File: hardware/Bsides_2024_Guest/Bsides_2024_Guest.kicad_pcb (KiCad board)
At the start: 2 copper layers, 0 parts

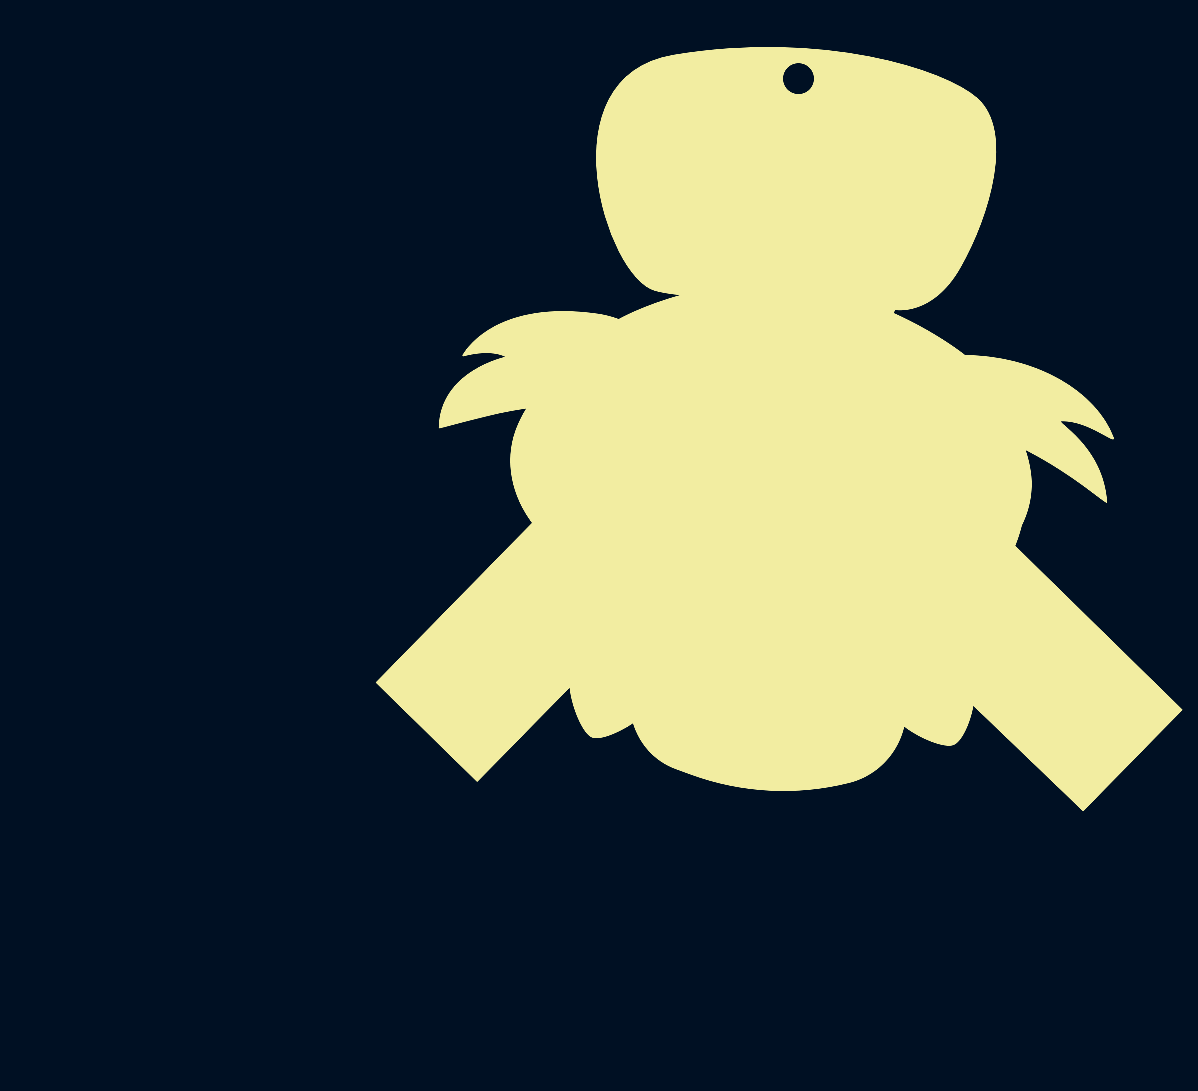
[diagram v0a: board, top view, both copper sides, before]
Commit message: feat(Hw):Added_Guest_And_Sponsor_Floorplan_and_3d_Models
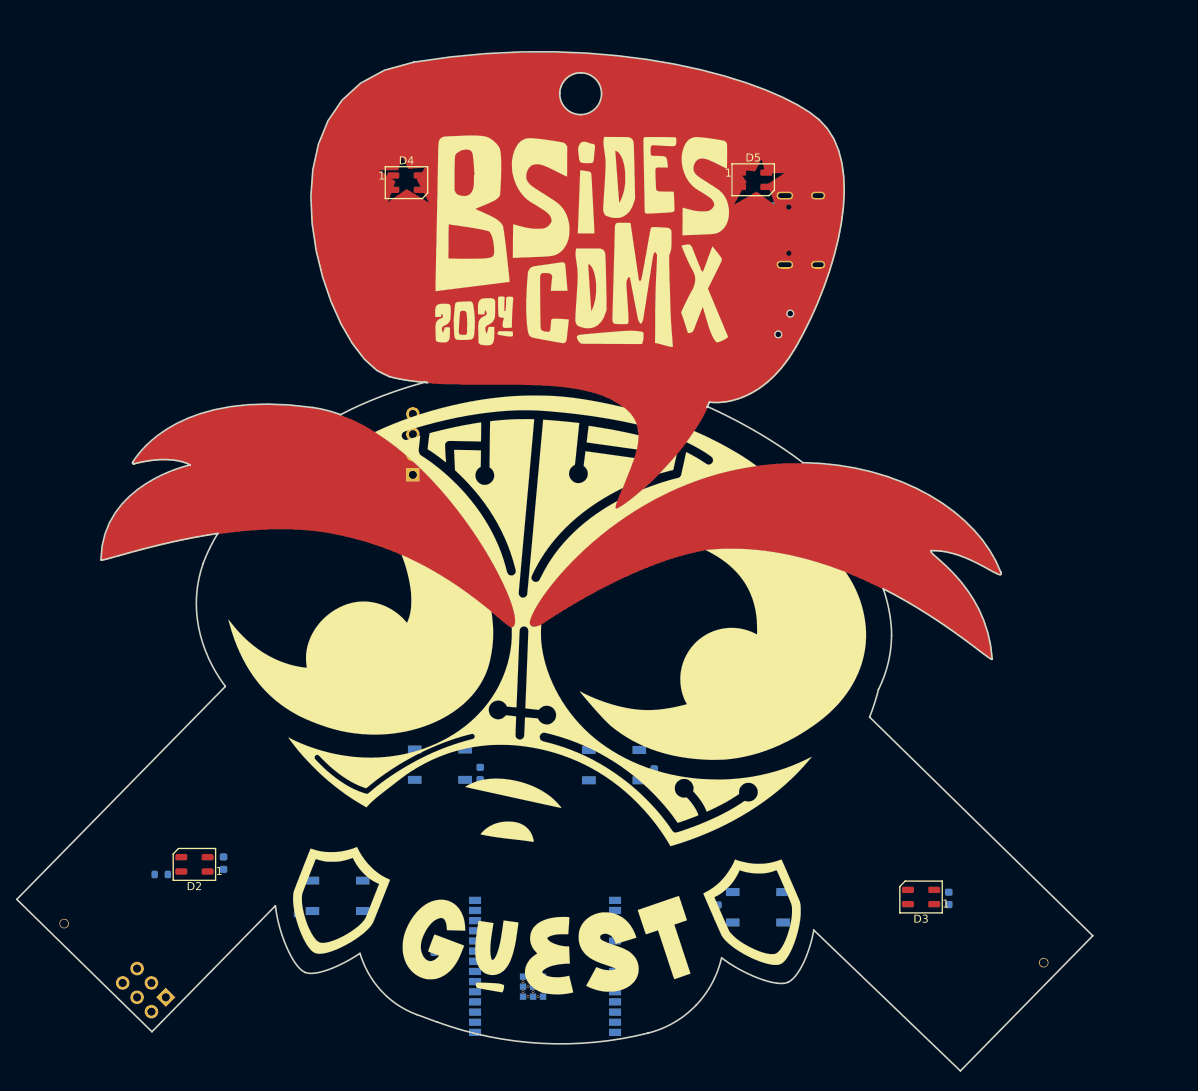
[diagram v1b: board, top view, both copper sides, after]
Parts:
- added C1: 10uF, Capacitor_SMD:C_0603_1608Metric, B.Cu at (149.0, 66.2)
- added C10: 0.1uF, Capacitor_SMD:C_0603_1608Metric, B.Cu at (116.2, 116.2)
- added C11: 0.1uF, Capacitor_SMD:C_0603_1608Metric, B.Cu at (145.9, 133.4)
- added C12: 0.1uF, Capacitor_SMD:C_0603_1608Metric, B.Cu at (146.8, 41.7)
- added C2: 10uF, Capacitor_SMD:C_0603_1608Metric, B.Cu at (143.4, 66.2)
- added C3: 0.1uF, Capacitor_SMD:C_0603_1608Metric, B.Cu at (168.6, 90.5)
- added C4: 0.1uF, Capacitor_SMD:C_0603_1608Metric, B.Cu at (85.2, 79.4)
- added C5: 0.1uF, Capacitor_SMD:C_0603_1608Metric, B.Cu at (84.1, 127.4)
- added C6: 0.1uF, Capacitor_SMD:C_0603_1608Metric, B.Cu at (174.8, 131.8)
- added C7: 0.1uF, Capacitor_SMD:C_0603_1608Metric, B.Cu at (103.5, 42.5)
- added C8: 0.1uF, Capacitor_SMD:C_0603_1608Metric, B.Cu at (137.9, 116.4)
- added C9: 0.1uF, Capacitor_SMD:C_0603_1608Metric, B.Cu at (93.3, 133.0)
- added D1: MBR120, Diode_SMD:D_SOD-123F, B.Cu at (144.0, 60.4)
- added D2: WS2812B, LED_SMD:LED_WS2812B-Mini_PLCC4_3.5x3.5mm, F.Cu at (80.5, 127.6)
- added D3: WS2812B, LED_SMD:LED_WS2812B-Mini_PLCC4_3.5x3.5mm, F.Cu at (171.3, 131.7)
- added D4: WS2812B, LED_SMD:LED_WS2812B-Mini_PLCC4_3.5x3.5mm, F.Cu at (107.0, 42.4)
- added D5: WS2812B, LED_SMD:LED_WS2812B-Mini_PLCC4_3.5x3.5mm, F.Cu at (150.3, 42.0)
- added F1: 0.5A, Fuse:Fuse_0805_2012Metric, B.Cu at (148.8, 51.8)
- added J1: Conn_02x03_Odd_Even, Connector_PinSocket_2.54mm:PinSocket_2x03_P2.54mm_Vertical, B.Cu at (76.9, 144.2)
- added J2: Battery, bsides:BH-AAA-A1aj001, B.Cu at (170.5, 123.8)
- added J3: Battery, bsides:BH-AAA-A1aj001, B.Cu at (80.3, 118.9)
- added J4: OLED, bsides:Display OLED 128 x32, B.Cu at (107.8, 78.9)
- added P1: USB_C_Plug_USB2.0, bsides:C393939, B.Cu at (154.3, 48.3)
- added Q1: DMG3415U-7, Package_TO_SOT_SMD:SOT-23, B.Cu at (146.9, 58.7)
- added R1: 3.3K, Resistor_SMD:R_0603_1608Metric, B.Cu at (110.4, 139.5)
- added R2: 100K, Resistor_SMD:R_0603_1608Metric, B.Cu at (142.1, 59.8)
- added R3: 5k1, Resistor_SMD:R_0603_1608Metric, B.Cu at (148.9, 49.2)
- added R4: 5k1, Resistor_SMD:R_0603_1608Metric, B.Cu at (148.9, 46.7)
- added R5: 10K, Resistor_SMD:R_0603_1608Metric, B.Cu at (88.3, 79.5)
- added R6: 470, Resistor_SMD:R_0603_1608Metric, B.Cu at (76.3, 128.9)
- added Ref**: Val**, Guest:Badge Guest, F.Cu at (125.6, 89.8)
- added SW1: ON, bsides:MSK12C02, B.Cu at (154.2, 60.0)
- added SW2: RESET, Button_Switch_SMD:SW_SPST_TL3342, B.Cu at (88.3, 75.5)
- added SW3: BOOT, Button_Switch_SMD:SW_SPST_TL3342, B.Cu at (167.8, 85.6)
- added SW4: RESET, Button_Switch_SMD:SW_SPST_TL3342, B.Cu at (132.9, 115.2)
- added SW5: ~, Button_Switch_SMD:SW_SPST_TL3342, B.Cu at (98.3, 131.5)
- added SW6: RESET, Button_Switch_SMD:SW_SPST_TL3342, B.Cu at (111.1, 115.1)
- added SW7: ~, Button_Switch_SMD:SW_SPST_TL3342, B.Cu at (150.9, 133.0)
- added U1: ESP32-C6-WROOM-1U-N4, bsides:XCVR_ESP32-C6-WROOM-1-N8, B.Cu at (124.3, 143.3)
- added U2: AP2112K-3.3, Package_TO_SOT_SMD:SOT-23-5, B.Cu at (146.2, 66.4)
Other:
- board outline added: 134.5 x 127.4 mm

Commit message: feat(Hw): Shitty Addon PCB added
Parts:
- added C13: 1uF, Capacitor_SMD:C_0603_1608Metric, B.Cu at (113.3, 145.6)
- added C14: 10uF, Capacitor_SMD:C_0603_1608Metric, B.Cu at (111.9, 145.6)
- added C15: 10uF, Capacitor_SMD:C_0603_1608Metric, B.Cu at (110.4, 145.6)
- J1: moved to F.Cu
- moved C10 10.5 mm to (105.8, 115.1)
- moved C11 10.3 mm to (156.2, 133.0)
- moved C3 8.02 mm to (162.2, 85.6), turned to -90 degrees
- moved C6 5.97 mm to (169.8, 135.1), turned to 0 degrees
- moved R2 4.79 mm to (145.2, 56.2), turned to 0 degrees
- moved R6 4.09 mm to (79.7, 131.2), turned to 180 degrees
- moved R4 3.91 mm to (149.0, 50.6)
- moved Q1 3.50 mm to (143.5, 59.2), turned to 180 degrees
- moved D1 2.83 mm to (146.6, 59.2)
- moved R1 2.71 mm to (110.4, 136.8)
- moved C2 2.64 mm to (140.9, 65.2)
- moved U2 2.55 mm to (143.9, 65.4)
- moved J1 2.43 mm to (75.1, 145.8), turned to -134.5 degrees
- moved C1 2.42 mm to (146.8, 65.2)
- moved U1 1.74 mm to (124.8, 141.7)
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
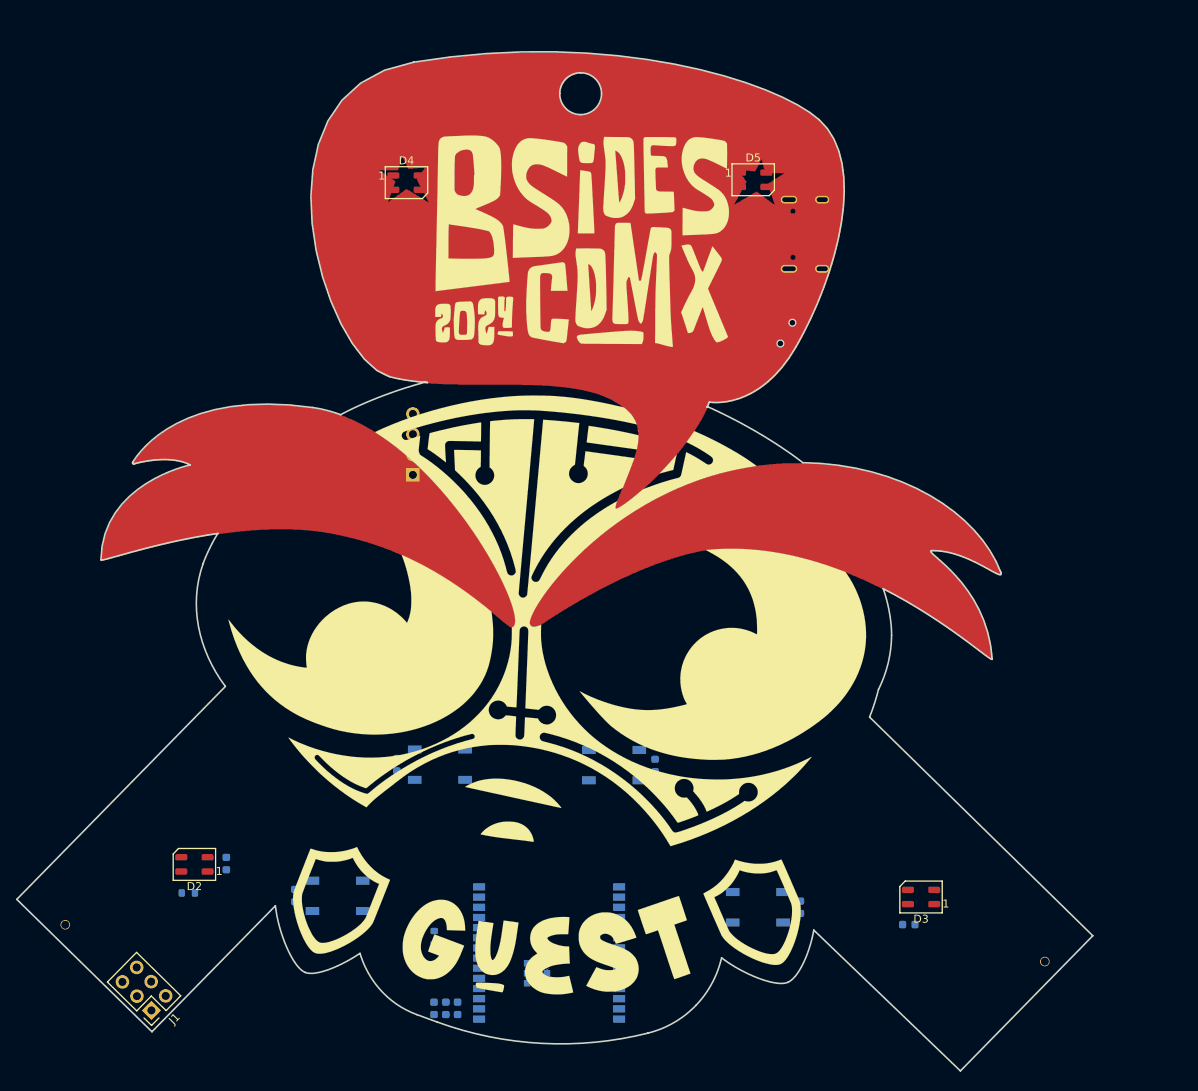
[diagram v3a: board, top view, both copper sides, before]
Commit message: feat(Hw): Start new floorplan
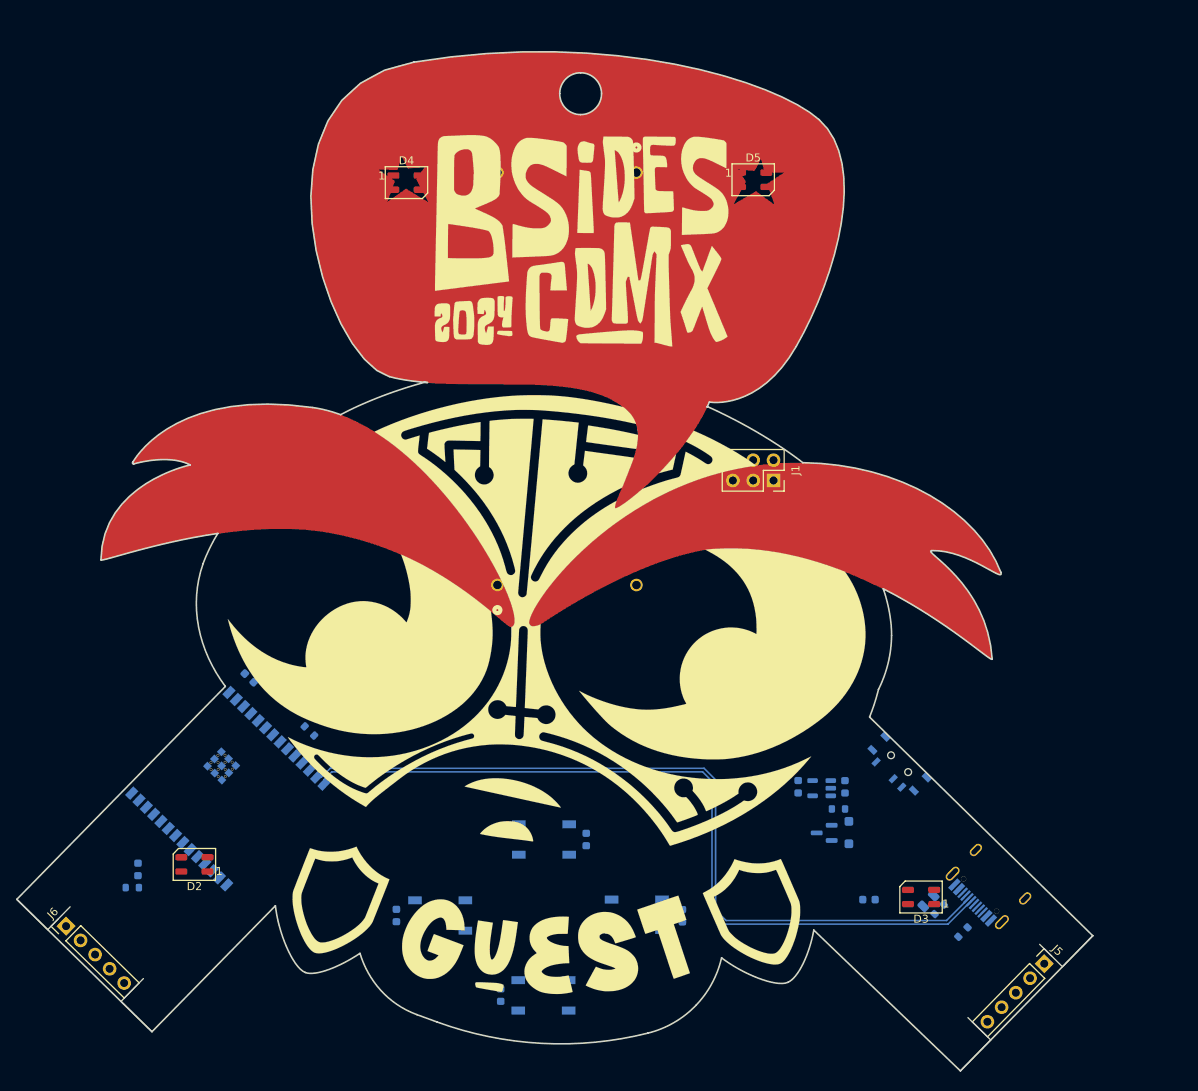
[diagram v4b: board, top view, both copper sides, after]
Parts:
- added J5: Conn_01x05, Connector_PinHeader_2.54mm:PinHeader_1x05_P2.54mm_Vertical, F.Cu at (186.7, 140.0)
- added J6: Conn_01x05, Connector_PinHeader_2.54mm:PinHeader_1x05_P2.54mm_Vertical, F.Cu at (64.4, 135.3)
- J2, J3: footprint bsides:BH-AAA-A1aj001 -> Guest:BATT_8BH-AA-A1AJ020_MYG
- moved J1 102.1 mm to (152.8, 79.6), turned to -90 degrees
- moved R4 89.8 mm to (176.5, 136.1), turned to 45.5 degrees
- moved J2 89.7 mm to (135.7, 41.1), turned to 90 degrees
- moved R3 89.0 mm to (173.6, 133.2), turned to 45.5 degrees
- moved P1 86.2 mm to (178.3, 131.8), turned to -44.5 degrees
- moved F1 83.2 mm to (172.2, 132.2), turned to -134.5 degrees
- moved D1 66.3 mm to (162.3, 123.6)
- moved R2 66.3 mm to (161.0, 120.7)
- moved Q1 66.3 mm to (159.2, 123.7)
- moved SW1 55.6 mm to (168.6, 115.0), turned to -44.5 degrees
- moved C1 54.8 mm to (161.8, 117.9)
- moved C2 54.8 mm to (155.9, 117.9)
- moved U2 54.8 mm to (158.9, 118.1)
- moved U1 49.5 mm to (82.5, 116.1), turned to -134 degrees
- moved C13 48.8 mm to (87.3, 104.3), turned to 136 degrees
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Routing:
- net /D-: track 0.00 -> 100.5 mm
- net /D+: track 0.00 -> 100.5 mm
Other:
- outline, holes or cut-outs redrawn

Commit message: feat(Hw): Update PCB
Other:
- outline, holes or cut-outs redrawn
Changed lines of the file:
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@@
 		(fp_arc
 			(start -2.500001 3.299999)
-			(mid -2.449999 3.249997)
+			(mid -2.45 3.249996)
 			(end -2.4 3.300001)
 			(stroke
@@
 		(fp_arc
 			(start -2.500001 3.299999)
-			(mid -2.449999 3.249997)
+			(mid -2.45 3.249996)
 			(end -2.4 3.300001)
 			(stroke
@@
 		(fp_arc
 			(start -2.4 3.300001)
-			(mid -2.450001 3.349998)
+			(mid -2.45 3.349997)
 			(end -2.500001 3.299999)
 			(stroke
@@
 		(layer "Edge.Cuts")
 	)
-	(gr_line
-		(start 71.276522 144.729814)
-		(end 74.075973 141.872705)
-		(stroke
-			(width 0.05)
-			(type default)
-		)
-		(layer "Edge.Cuts")
-	)
 	(gr_curve
 		(pts
@@
 		(layer "Edge.Cuts")
 	)
-	(gr_line
-		(start 188.961906 140.388346)
-		(end 186.104797 137.588895)
-		(stroke
-			(width 0.05)
-			(type default)
-		)
-		(layer "Edge.Cuts")
-	)
 	(gr_curve
 		(pts
@@
 		(layer "Edge.Cuts")
 	)
-	(gr_line
-		(start 192.750825 136.520175)
-		(end 188.961906 140.388346)
-		(stroke
-			(width 0.05)
-			(type default)
-		)
-		(layer "Edge.Cuts")
-	)
 	(gr_curve
 		(pts
@@
 	)
 	(gr_line
-		(start 176.202092 153.414868)
-		(end 179.991011 149.546697)
-		(stroke
-			(width 0.05)
-			(type default)
-		)
-		(layer "Edge.Cuts")
-	)
-	(gr_line
-		(start 58.25 131.97)
-		(end 62.118171 135.758919)
-		(stroke
-			(width 0.05)
-			(type default)
-		)
-		(layer "Edge.Cuts")
-	)
-	(gr_line
 		(start 58.25 131.97)
 		(end 75.144693 148.518733)
@@
 		(layer "Edge.Cuts")
 	)
-	(gr_line
-		(start 64.917622 132.90181)
-		(end 62.118171 135.758919)
-		(stroke
-			(width 0.05)
-			(type default)
-		)
-		(layer "Edge.Cuts")
-	)
 	(gr_curve
 		(pts
@@
 		(layer "Edge.Cuts")
 	)
-	(gr_line
-		(start 75.144693 148.518733)
-		(end 71.276522 144.729814)
-		(stroke
-			(width 0.05)
-			(type default)
-		)
-		(layer "Edge.Cuts")
-	)
 	(gr_curve
 		(pts
@@
 			(type default)
 		)
-		(layer "Edge.Cuts")
-	)
-	(gr_line
-		(start 177.133902 146.747246)
-		(end 179.991011 149.546697)
-		(stroke
-			(width 0.05)
-			(type default)
-		)

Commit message: feat(Hw): Update PCB
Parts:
- moved J1 5.24 mm to (148.4, 76.9), turned to -117.5 degrees
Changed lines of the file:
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@@
 	(footprint "Connector_PinSocket_2.54mm:PinSocket_2x03_P2.54mm_Vertical"
 		(layer "F.Cu")
-		(at 152.84 79.61 -90)
+		(at 148.384047 76.85016 -117.5)
 		(descr "Through hole straight socket strip, 2x03, 2.54mm pitch, double cols (from Kicad 4.0.7), script generated")
 		(tags "Through hole socket strip THT 2x03 2.54mm double row")
 		(property "Reference" "J1"
-			(at -1.27 -2.769999 90)
+			(at -1.27 -2.769999 -117.5)
 			(layer "F.SilkS")
 			(effects
@@
 		)
 		(property "Value" "Conn_02x03_Odd_Even"
-			(at -1.27 7.850001 90)
+			(at -1.269999 7.850001 -117.5)
 			(layer "F.Fab")
 			(effects
@@
 		)
 		(property "Footprint" "Connector_PinSocket_2.54mm:PinSocket_2x03_P2.54mm_Vertical"
-			(at 0 0 -90)
+			(at 0 0 -117.5)
 			(unlocked yes)
 			(layer "F.Fab")
@@
 		)
 		(property "Datasheet" ""
-			(at 0 0 -90)
+			(at 0 0 -117.5)
 			(unlocked yes)
 			(layer "F.Fab")
@@
 		)
 		(property "Description" "Generic connector, double row, 02x03, odd/even pin numbering scheme (row 1 odd numbers, row 2 even numbers), script generated (kicad-library-utils/schlib/autogen/connector/)"
-			(at 0 0 -90)
+			(at 0 0 -117.5)
 			(unlocked yes)
 			(layer "F.Fab")
@@
 		(attr through_hole)
 		(fp_line
-			(start -3.870001 6.41)
-			(end 1.33 6.409999)
+			(start -3.869999 6.41)
+			(end 1.330001 6.409998)
 			(stroke
 				(width 0.12)
@@
 		)
 		(fp_line
-			(start 1.33 1.270001)
-			(end 1.33 6.409999)
+			(start 1.330001 1.27)
+			(end 1.330001 6.409998)
 			(stroke
 				(width 0.12)
@@
 		(fp_line
 			(start -1.27 1.27)
-			(end 1.33 1.270001)
+			(end 1.330001 1.27)
 			(stroke
 				(width 0.12)
@@
 		)
 		(fp_line
-			(start -3.87 -1.33)
-			(end -3.870001 6.41)
+			(start 1.33 -1.33)
+			(end 1.330001 0)
 			(stroke
 				(width 0.12)
@@
 		)
 		(fp_line
-			(start -3.87 -1.33)
-			(end -1.27 -1.33)
+			(start 0 -1.330001)
+			(end 1.33 -1.33)
 			(stroke
 				(width 0.12)
@@
 		)
 		(fp_line
-			(start 0 -1.33)
-			(end 1.33 -1.33)
+			(start -3.870001 -1.33)
+			(end -3.869999 6.41)
 			(stroke
 				(width 0.12)
@@
 		)
 		(fp_line
-			(start 1.33 -1.33)
-			(end 1.33 0)
+			(start -3.870001 -1.33)
+			(end -1.27 -1.33)
 			(stroke
 				(width 0.12)
@@
 		)
 		(fp_line
-			(start -4.340001 6.85)
-			(end -4.34 -1.8)
+			(start 1.759999 6.850001)
+			(end -4.340001 6.849999)
 			(stroke
 				(width 0.05)
@@
 		)
 		(fp_line
-			(start 1.76 6.85)
-			(end -4.340001 6.85)
+			(start -4.340001 6.849999)
+			(end -4.339998 -1.8)
 			(stroke
 				(width 0.05)
@@
 		)
 		(fp_line
-			(start 1.76 -1.799999)
-			(end 1.76 6.85)
+			(start 1.760001 -1.799999)
+			(end 1.759999 6.850001)
 			(stroke
 				(width 0.05)
@@
 		)
 		(fp_line
-			(start -4.34 -1.8)
-			(end 1.76 -1.799999)
+			(start -4.339998 -1.8)
+			(end 1.760001 -1.799999)
 			(stroke
 				(width 0.05)
@@
 		)
 		(fp_line
-			(start -3.81 6.35)
-			(end -3.809999 -1.27)
+			(start 1.270001 6.349999)
+			(end -3.81 6.35)
 			(stroke
 				(width 0.1)
@@
 		)
 		(fp_line
-			(start 1.27 6.349999)
-			(end -3.81 6.35)
+			(start -3.81 6.35)
+			(end -3.809999 -1.270001)
 			(stroke
 				(width 0.1)
@@
 		)
 		(fp_line
-			(start 1.269999 -0.27)
-			(end 1.27 6.349999)
+			(start 1.269999 -0.269999)
+			(end 1.270001 6.349999)
 			(stroke
 				(width 0.1)
@@
 		)
 		(fp_line
-			(start -3.809999 -1.27)
-			(end 0.269999 -1.27)
+			(start 0.27 -1.27)
+			(end 1.269999 -0.269999)
 			(stroke
 				(width 0.1)
@@
 		)
 		(fp_line
-			(start 0.269999 -1.27)
-			(end 1.269999 -0.27)
+			(start -3.809999 -1.270001)
+			(end 0.27 -1.27)
 			(stroke
 				(width 0.1)
@@
 		)
 		(fp_text user "${REFERENCE}"
-			(at -1.27 2.540001 180)
+			(at -1.27 2.54 152.5)
 			(layer "F.Fab")
 			(effects
@@
 		)
 		(pad "1" thru_hole rect
-			(at 0 0 270)
+			(at 0 0 242.5)
 			(size 1.7 1.7)
 			(drill 1)
@@
 		)
 		(pad "2" thru_hole oval
-			(at -2.54 0 270)
+			(at -2.540001 0 242.5)
 			(size 1.7 1.7)
 			(drill 1)
@@
 		)
 		(pad "3" thru_hole oval
-			(at 0 2.54 270)
+			(at 0 2.540001 242.5)
 			(size 1.7 1.7)
 			(drill 1)
@@
 		)
 		(pad "4" thru_hole oval
-			(at -2.539999 2.54 270)
+			(at -2.539998 2.539999 242.5)
 			(size 1.7 1.7)
 			(drill 1)
@@
 		)
 		(pad "5" thru_hole oval
-			(at 0 5.08 270)
+			(at 0.000001 5.08 242.5)
 			(size 1.7 1.7)
 			(drill 1)
@@
 		)
 		(pad "6" thru_hole oval
-			(at -2.54 5.080001 270)
+			(at -2.54 5.080002 242.5)
 			(size 1.7 1.7)
 			(drill 1)
@@
 		(fp_arc
 			(start -2.500001 3.299999)
-			(mid -2.45 3.249996)
+			(mid -2.449999 3.249996)
 			(end -2.4 3.300001)
 			(stroke
@@
 		(fp_arc
 			(start -2.500001 3.299999)
-			(mid -2.45 3.249996)
+			(mid -2.449999 3.249996)
 			(end -2.4 3.300001)
 			(stroke
@@
 		(fp_arc
 			(start -2.4 3.300001)
-			(mid -2.45 3.349997)
+			(mid -2.45 3.349996)
 			(end -2.500001 3.299999)
 			(stroke
